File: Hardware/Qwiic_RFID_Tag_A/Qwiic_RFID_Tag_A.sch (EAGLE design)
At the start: 26 parts, among them J1 Qwiic, J2 Qwiic, U1 ST25DV64KC

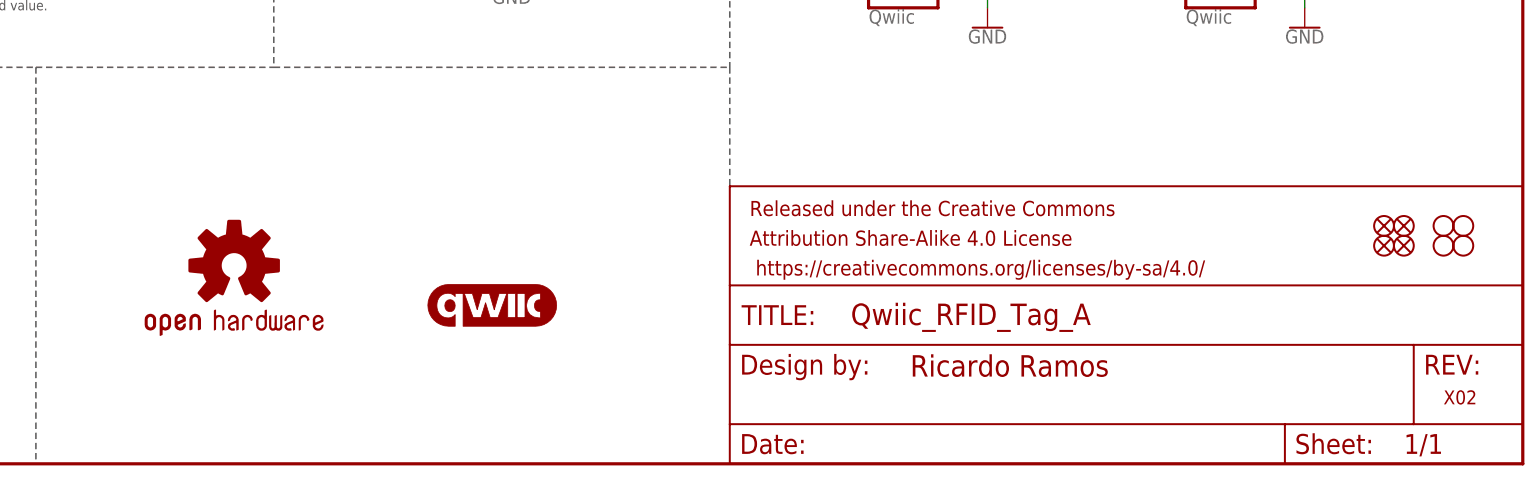
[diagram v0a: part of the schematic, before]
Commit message: Update aesthetics
Add SFE logo
Update version number
Change schematic frame to correct version
Update design attribution
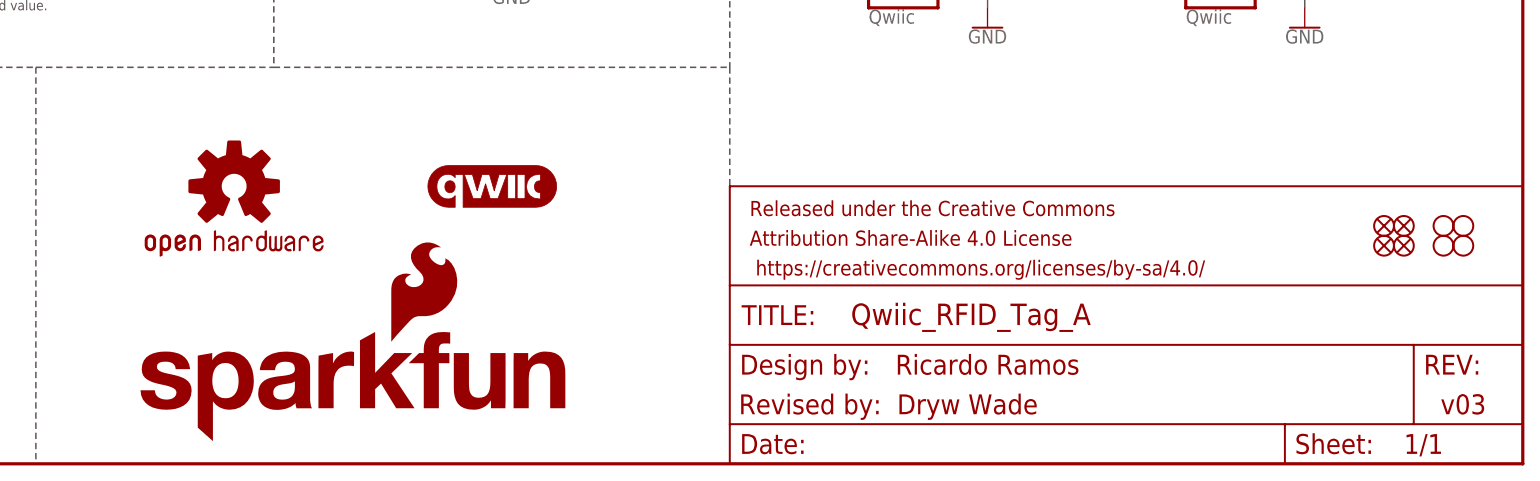
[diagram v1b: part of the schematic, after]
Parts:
- removed FRAME1: FRAME-LETTERNO_PACKAGE, SparkFun-Aesthetics:FRAME-LETTERNO_PACKAGE
- added FRAME2: FRAME-LETTER, SparkFun-Aesthetics:FRAME-LETTER
- added LOGO2: SFE_LOGO_NAME_FLAME.1_INCH, SparkFun-Aesthetics:SFE_LOGO_NAME_FLAME.1_INCH
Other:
- note added: "Revised by: Dryw Wade"
- note added: "Ricardo Ramos"
- note added: "v03"
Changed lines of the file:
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@@
 <part name="J1" library="SparkFun-Connectors" deviceset="QWIIC_CONNECTOR" device="JS-1MM" value="Qwiic"/>
 <part name="J2" library="SparkFun-Connectors" deviceset="QWIIC_CONNECTOR" device="JS-1MM" value="Qwiic"/>
-<part name="FRAME1" library="SparkFun-Aesthetics" deviceset="FRAME-LETTER" device="NO_PACKAGE">
-<attribute name="DESIGNER" value="Ricardo Ramos"/>
-<attribute name="REV" value="X02"/>
-<attribute name="VERSION" value="x01"/>
-</part>
 <part name="L1" library="QWIIC_RFID_TAG_COILS" deviceset="PCB_COIL_4UH" device="_A"/>
 <part name="C2" library="SparkFun-Capacitors" deviceset="4.7PF" device="-0603-50V-5%" value="4.7pF"/>
@@
 <part name="H3" library="SparkFun-Hardware" deviceset="STAND-OFF" device=""/>
 <part name="H4" library="SparkFun-Hardware" deviceset="STAND-OFF" device=""/>
+<part name="FRAME2" library="SparkFun-Aesthetics" deviceset="FRAME-LETTER" device=""/>
+<part name="LOGO2" library="SparkFun-Aesthetics" deviceset="SFE_LOGO_NAME_FLAME" device=".1_INCH"/>
 </parts>
 <sheets>
@@
 <wire x1="58.42" y1="50.8" x2="58.42" y2="0" width="0.2032" layer="97" style="longdash"/>
 <wire x1="147.32" y1="50.8" x2="147.32" y2="35.56" width="0.2032" layer="97" style="longdash"/>
+<text x="241.3" y="7.62" size="2.54" layer="94" font="vector" align="center">v03</text>
+<text x="180.34" y="12.7" size="2.54" layer="94" font="vector" align="center">Ricardo Ramos</text>
+<text x="167.64" y="7.62" size="2.54" layer="94" font="vector" align="center">Revised by:  Dryw Wade</text>
 </plain>
 <instances>
@@
 <attribute name="VALUE" x="205.74" y="58.166" size="1.778" layer="96" font="vector" align="top-left"/>
 <attribute name="NAME" x="205.74" y="71.374" size="1.778" layer="95" font="vector"/>
-</instance>
-<instance part="FRAME1" gate="G$1" x="0" y="0" smashed="yes">
-<attribute name="REV" x="238.76" y="7.62" size="1.778" layer="94" font="vector"/>
-</instance>
-<instance part="FRAME1" gate="V" x="147.32" y="0" smashed="yes">
-<attribute name="LAST_DATE_TIME" x="160.02" y="1.27" size="2.54" layer="94" font="vector"/>
-<attribute name="SHEET" x="233.68" y="1.27" size="2.54" layer="94" font="vector"/>
-<attribute name="DRAWING_NAME" x="162.814" y="17.78" size="2.7432" layer="94" font="vector"/>
-<attribute name="DESIGNER" x="170.434" y="11.176" size="2.7432" layer="94" font="vector"/>
 </instance>
 <instance part="L1" gate="G$1" x="45.72" y="76.2" smashed="yes" rot="MR180">
@@
 <instance part="FD3" gate="G$1" x="231.14" y="30.48" smashed="yes"/>
 <instance part="FD4" gate="G$1" x="233.68" y="30.48" smashed="yes"/>
-<instance part="LOGO1" gate="G$1" x="83.82" y="25.4" smashed="yes"/>
-<instance part="LOGO3" gate="G$1" x="116.84" y="20.32" smashed="yes"/>
+<instance part="LOGO1" gate="G$1" x="83.82" y="35.56" smashed="yes"/>
+<instance part="LOGO3" gate="G$1" x="116.84" y="35.56" smashed="yes"/>
 <instance part="H1" gate="G$1" x="238.76" y="27.94" smashed="yes"/>
 <instance part="H2" gate="G$1" x="241.3" y="27.94" smashed="yes"/>
 <instance part="H3" gate="G$1" x="238.76" y="30.48" smashed="yes"/>
 <instance part="H4" gate="G$1" x="241.3" y="30.48" smashed="yes"/>
+<instance part="FRAME2" gate="G$1" x="0" y="0" smashed="yes"/>
+<instance part="FRAME2" gate="V" x="147.32" y="0" smashed="yes">
+<attribute name="LAST_DATE_TIME" x="160.02" y="1.27" size="2.54" layer="94" font="vector"/>
+<attribute name="SHEET" x="233.68" y="1.27" size="2.54" layer="94" font="vector"/>
+<attribute name="DRAWING_NAME" x="162.814" y="17.78" size="2.7432" layer="94" font="vector"/>
+<attribute name="DESIGNER" x="170.434" y="11.176" size="2.7432" layer="94" font="vector"/>
+<attribute name="REV" x="236.22" y="6.604" size="2.7432" layer="94" font="vector"/>
+</instance>
+<instance part="LOGO2" gate="G$1" x="71.12" y="2.54" smashed="yes"/>
 </instances>
 <busses>

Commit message: Design review updates
All scehmatics:
Change IC text to “Dynamic RFID Tag - ST25DV64KC”
Move decoupling capacitor near IC
Update I2C jumper text to say "traces" instead of "trace"

Version A board:
Fix stray via diameter
Approve jumper overlap error

Version C board:
Add SFE logo to bottom silk
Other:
- note added: "Cut traces to disable I2C pullups"
- note added: "Dynamic RFID Tag - ST25DV64KC"
- note removed: "Cut trace to disable I2C pullups"
- note removed: "Power decoupling"
- note removed: "ST25DV64KC Dynamic RFID Tag"
- moved on the sheet: C1
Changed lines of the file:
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@@
 <text x="172.72" y="172.72" size="2.54" layer="94" font="vector" align="center">Power LED</text>
 <text x="223.52" y="172.72" size="2.54" layer="94" font="vector" align="center">!GPO! Pullup</text>
-<text x="45.72" y="170.18" size="2.54" layer="94" font="vector" align="center">ST25DV64KC Dynamic RFID Tag</text>
-<text x="27.94" y="40.64" size="2.54" layer="94" font="vector" align="center">Power decoupling</text>
+<text x="45.72" y="170.18" size="2.54" layer="94" font="vector" align="center">Dynamic RFID Tag - ST25DV64KC</text>
 <wire x1="0" y1="104.14" x2="88.9" y2="104.14" width="0.2032" layer="97" style="longdash"/>
 <wire x1="88.9" y1="104.14" x2="198.12" y2="104.14" width="0.2032" layer="97" style="longdash"/>
@@
 <wire x1="88.9" y1="104.14" x2="88.9" y2="185.42" width="0.2032" layer="97" style="longdash"/>
 <wire x1="0" y1="48.26" x2="0" y2="50.8" width="0.2032" layer="97" style="longdash"/>
-<wire x1="0" y1="50.8" x2="58.42" y2="50.8" width="0.2032" layer="97" style="longdash"/>
-<wire x1="58.42" y1="50.8" x2="88.9" y2="50.8" width="0.2032" layer="97" style="longdash"/>
+<wire x1="0" y1="50.8" x2="88.9" y2="50.8" width="0.2032" layer="97" style="longdash"/>
 <wire x1="88.9" y1="50.8" x2="147.32" y2="50.8" width="0.2032" layer="97" style="longdash"/>
 <wire x1="88.9" y1="104.14" x2="88.9" y2="50.8" width="0.2032" layer="97" style="longdash"/>
 <wire x1="147.32" y1="185.42" x2="147.32" y2="50.8" width="0.2032" layer="97" style="longdash"/>
 <wire x1="198.12" y1="104.14" x2="198.12" y2="185.42" width="0.2032" layer="97" style="longdash"/>
-<text x="104.14" y="168.91" size="1.27" layer="97" font="vector">Cut trace to disable I2C pullups</text>
+<text x="104.14" y="168.91" size="1.27" layer="97" font="vector">Cut traces to disable I2C pullups</text>
 <text x="45.72" y="59.69" size="1.27" layer="97" font="vector" align="center">C2 may be changed to improve circuit resonance.
 5.6 pF is the initial calculated value.</text>
-<wire x1="58.42" y1="50.8" x2="58.42" y2="0" width="0.2032" layer="97" style="longdash"/>
 <wire x1="147.32" y1="50.8" x2="147.32" y2="35.56" width="0.2032" layer="97" style="longdash"/>
 <text x="241.3" y="7.62" size="2.54" layer="94" font="vector" align="center">v03</text>
@@
 <attribute name="VALUE" x="226.568" y="147.32" size="1.778" layer="96" font="vector" rot="R90" align="center" display="off"/>
 </instance>
-<instance part="C1" gate="G$1" x="27.94" y="20.32" smashed="yes">
-<attribute name="NAME" x="29.464" y="23.241" size="1.778" layer="95" font="vector"/>
-<attribute name="VALUE" x="29.464" y="18.161" size="1.778" layer="96" font="vector"/>
+<instance part="C1" gate="G$1" x="12.7" y="137.16" smashed="yes">
+<attribute name="NAME" x="14.224" y="140.081" size="1.778" layer="95" font="vector"/>
+<attribute name="VALUE" x="14.224" y="135.001" size="1.778" layer="96" font="vector"/>
 </instance>
 <instance part="J3" gate="JP1" x="111.76" y="71.12" smashed="yes">
@@
 <attribute name="NAME" x="106.68" y="81.788" size="1.778" layer="95" font="vector"/>
 </instance>
-<instance part="SUPPLY1" gate="G$1" x="27.94" y="27.94" smashed="yes">
-<attribute name="VALUE" x="27.94" y="30.734" size="1.778" layer="96" align="bottom-center"/>
-</instance>
-<instance part="GND1" gate="1" x="27.94" y="12.7" smashed="yes">
-<attribute name="VALUE" x="27.94" y="12.446" size="1.778" layer="96" align="top-center"/>
+<instance part="SUPPLY1" gate="G$1" x="12.7" y="144.78" smashed="yes">
+<attribute name="VALUE" x="12.7" y="147.574" size="1.778" layer="96" align="bottom-center"/>
+</instance>
+<instance part="GND1" gate="1" x="12.7" y="129.54" smashed="yes">
+<attribute name="VALUE" x="12.7" y="129.286" size="1.778" layer="96" align="top-center"/>
 </instance>
 <instance part="SUPPLY3" gate="G$1" x="30.48" y="147.32" smashed="yes">
@@
 <instance part="FD3" gate="G$1" x="231.14" y="30.48" smashed="yes"/>
 <instance part="FD4" gate="G$1" x="233.68" y="30.48" smashed="yes"/>
-<instance part="LOGO1" gate="G$1" x="83.82" y="35.56" smashed="yes"/>
-<instance part="LOGO3" gate="G$1" x="116.84" y="35.56" smashed="yes"/>
+<instance part="LOGO1" gate="G$1" x="53.34" y="22.86" smashed="yes"/>
+<instance part="LOGO3" gate="G$1" x="27.94" y="22.86" smashed="yes"/>
 <instance part="H1" gate="G$1" x="238.76" y="27.94" smashed="yes"/>
 <instance part="H2" gate="G$1" x="241.3" y="27.94" smashed="yes"/>
@@
 <attribute name="REV" x="236.22" y="6.604" size="2.7432" layer="94" font="vector"/>
 </instance>
-<instance part="LOGO2" gate="G$1" x="71.12" y="2.54" smashed="yes"/>
+<instance part="LOGO2" gate="G$1" x="71.12" y="12.7" smashed="yes"/>
 </instances>
 <busses>
@@
 <segment>
 <pinref part="GND1" gate="1" pin="GND"/>
-<wire x1="27.94" y1="17.78" x2="27.94" y2="15.24" width="0.1524" layer="91"/>
+<wire x1="12.7" y1="134.62" x2="12.7" y2="132.08" width="0.1524" layer="91"/>
 <pinref part="C1" gate="G$1" pin="2"/>
 </segment>
@@
 </segment>
 <segment>
-<wire x1="27.94" y1="25.4" x2="27.94" y2="27.94" width="0.1524" layer="91"/>
+<wire x1="12.7" y1="142.24" x2="12.7" y2="144.78" width="0.1524" layer="91"/>
 <pinref part="SUPPLY1" gate="G$1" pin="3.3V"/>
 <pinref part="C1" gate="G$1" pin="1"/>

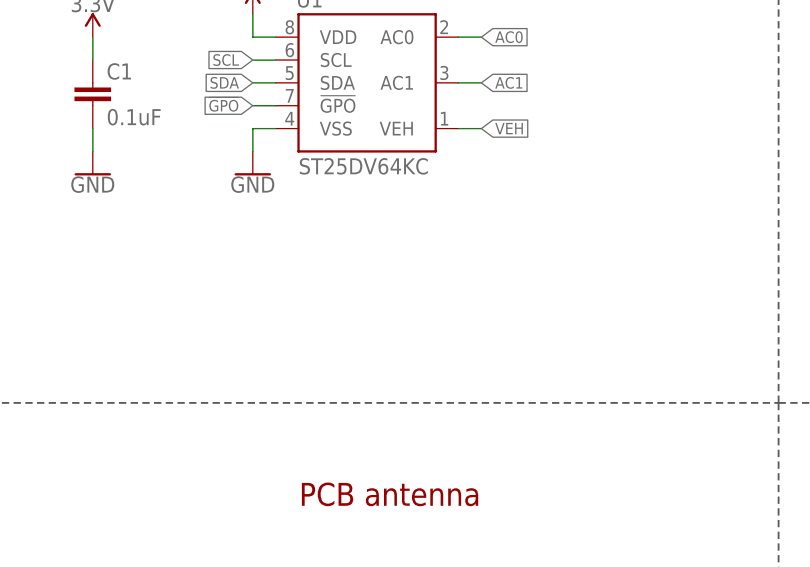
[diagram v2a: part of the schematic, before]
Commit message: Design review updates
Add version letter to silk
Add I2C addresses to schematic
Change PTH silk labels from "3.3V" to "3V3"
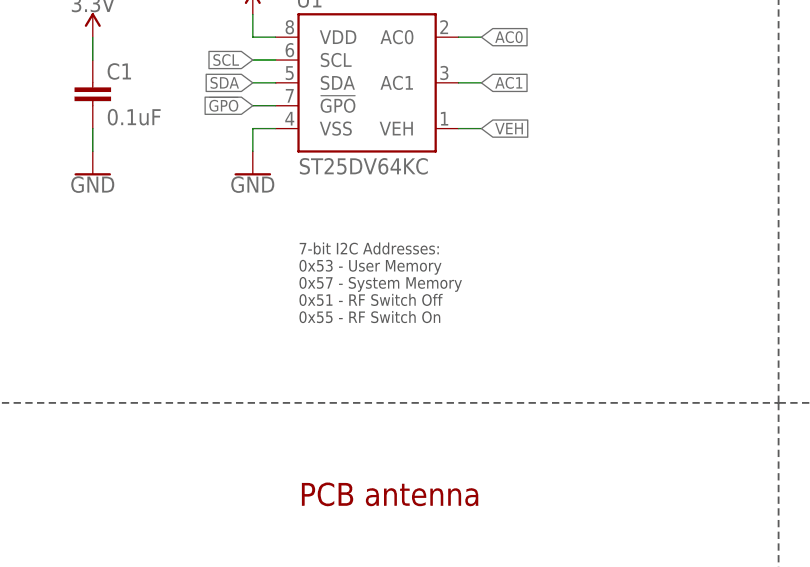
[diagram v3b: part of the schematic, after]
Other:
- note added: "7-bit I2C Addresses: 0x53 - User Memory 0x57 - System Memory 0x51 - RF Switch Off 0x55 - RF Switch On"
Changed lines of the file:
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@@
 <text x="180.34" y="12.7" size="2.54" layer="94" font="vector" align="center">Ricardo Ramos</text>
 <text x="167.64" y="7.62" size="2.54" layer="94" font="vector" align="center">Revised by:  Dryw Wade</text>
+<text x="35.56" y="113.03" size="1.27" layer="97" font="vector">7-bit I2C Addresses:
+0x53 - User Memory
+0x57 - System Memory
+0x51 - RF Switch Off
+0x55 - RF Switch On</text>
 </plain>
 <instances>
